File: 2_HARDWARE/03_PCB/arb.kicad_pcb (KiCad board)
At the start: 6 copper layers, 104.3 x 53.5 mm, 269 parts, among them J1 TYPE-C-31-M-12, J2 SMA, J3 SMA, J4 BNC, J5 PH-00244, SW1 TS-1187A-B-A-B, U1 TLV70333DBV, U10 LMK1C1103PWR, U11 STM32F446ZETx, U12 ICE40UP5K-SG48ITR, U13 93LC56BT-I_OT, U14 FT2232HL, U15 W25Q128JVSIQ, U16 W25Q128JVSIQ, U17 AD9850, U18 AD9744, U19 LM6171, U2 TLV76133DCY, U20 LM6171, U21 TMUX6104, U22 TPL0401B-10, U23 THS3491, U24 ADG1219BRJZ, U25 LM6171, U26 TMUX6104, U3 TLV70333DBV, U4 LM3880MF-1AA, U5 TLV70312DBV, U6 TLV70325DBV, U7 TPS65131RGE, U8 TPD2E001DRL, U9 ADG1219BRJZ, X1 ASE-10.000MHz, X2 ASE-100.000MHz, Y1 32.768k, Y2 12 MHz

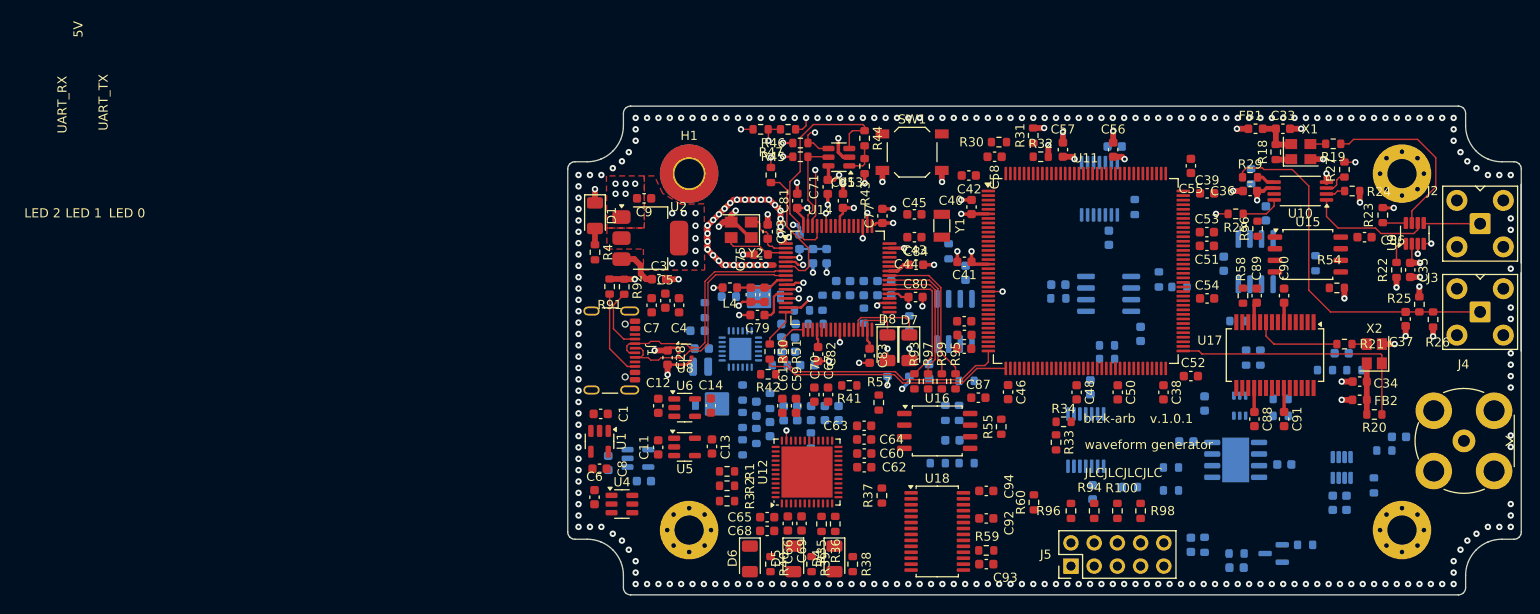
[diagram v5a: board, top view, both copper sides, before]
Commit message: MINOR: Added Power and GND Vias on the Top Layer.
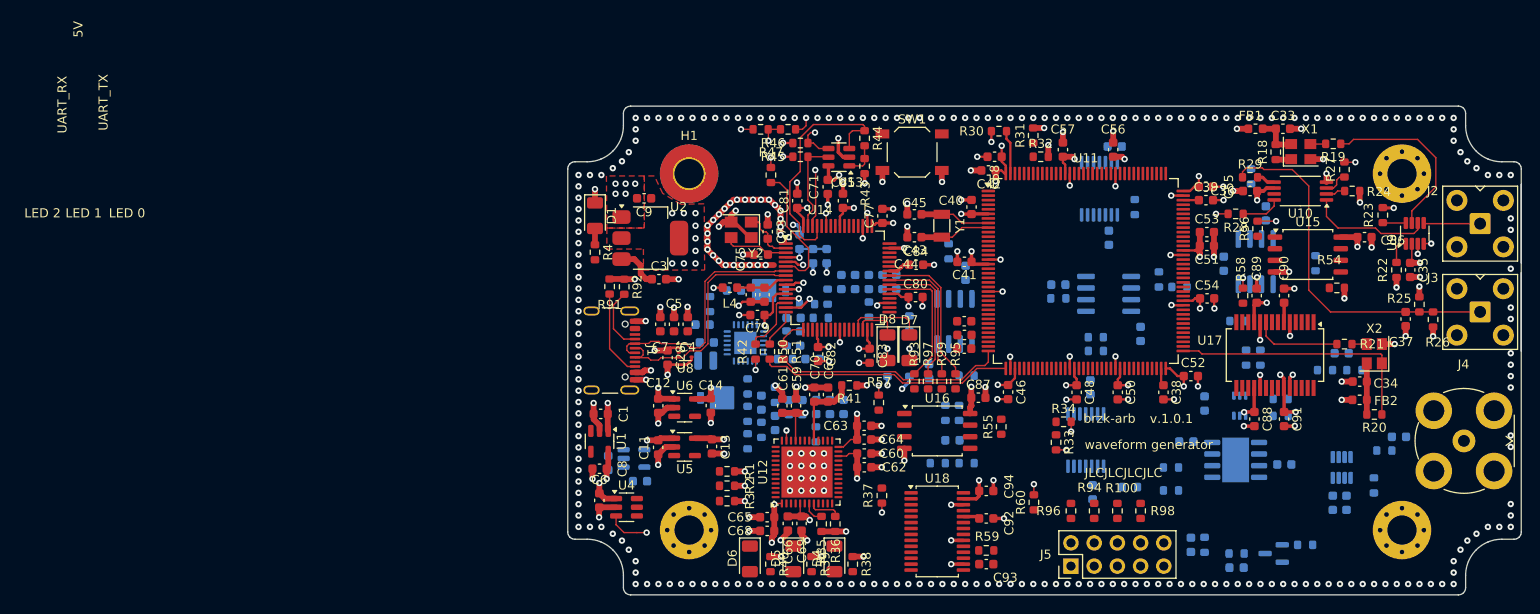
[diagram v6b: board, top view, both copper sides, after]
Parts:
- moved R42 2.83 mm to (116.4, 86.9), turned to 90 degrees
- moved C55 2.81 mm to (165.7, 68.8), turned to 0 degrees
- moved C5 2.74 mm to (107.5, 83.9)
- moved C4 2.28 mm to (109.0, 83.9)
- moved C7 2.28 mm to (106.0, 83.9)
- moved C42 2.22 mm to (141.8, 67.0)
- moved R85 1.51 mm to (153.6, 86.8)
- moved R88 1.51 mm to (153.6, 85.3)
- moved R30 1.20 mm to (143.0, 62.8)
- moved C16 0.87 mm to (110.6, 83.9)
- moved C25 0.87 mm to (127.3, 79.3)
- moved L1 0.87 mm to (110.9, 87.8)
- moved R17 0.87 mm to (128.8, 82.3)
- moved R5 0.87 mm to (111.4, 81.7)
- moved C19 0.87 mm to (117.0, 92.5)
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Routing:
- net GND: track 101.4 -> 193.0 mm, vias 303 -> 384
- net 3P3V_D: track 50.9 -> 115.4 mm, vias 32 -> 60
- net 3P3V_D_FPGA: track 0.00 -> 22.4 mm, vias 0 -> 7
- net 5P0V: track 8.85 -> 23.1 mm, vias 2 -> 7
- net Net-(U12D-VCCPLL): track 0.00 -> 8.57 mm
- net 1P2V_D: track 0.00 -> 8.39 mm, vias 0 -> 3
- net 2P5V_D: track 0.00 -> 8.13 mm, vias 0 -> 2
- net Net-(U11-PC15): track 0.00 -> 7.75 mm
- net Net-(U11-PC14): track 0.00 -> 7.71 mm
- net Net-(U14-~{RESET}): track 0.00 -> 6.80 mm
- net Net-(U11-PDR_ON): track 0.00 -> 4.81 mm
- net 3P3V_A: track 4.87 -> 8.92 mm, vias 0 -> 2
- net GPIO_FPGARST_MCU_FPGA_3P3_L: track 0.00 -> 3.54 mm
- net GPIO_CFG_DONE_FPGA_MCU_3P3: track 0.00 -> 2.43 mm
- net Net-(U11-VCAP_1): track 0.00 -> 1.94 mm
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
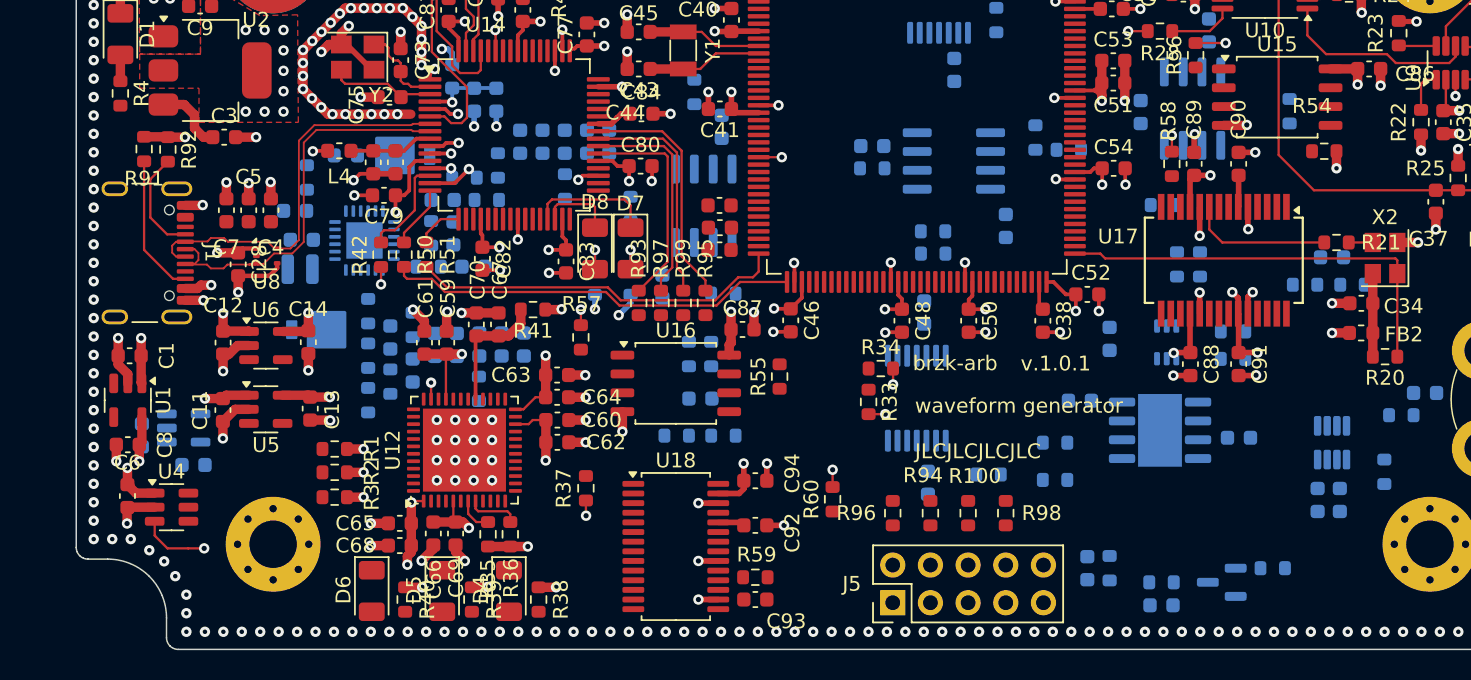
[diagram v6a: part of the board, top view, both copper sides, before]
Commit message: MINOR: Routed Layer 3 Power Planes.
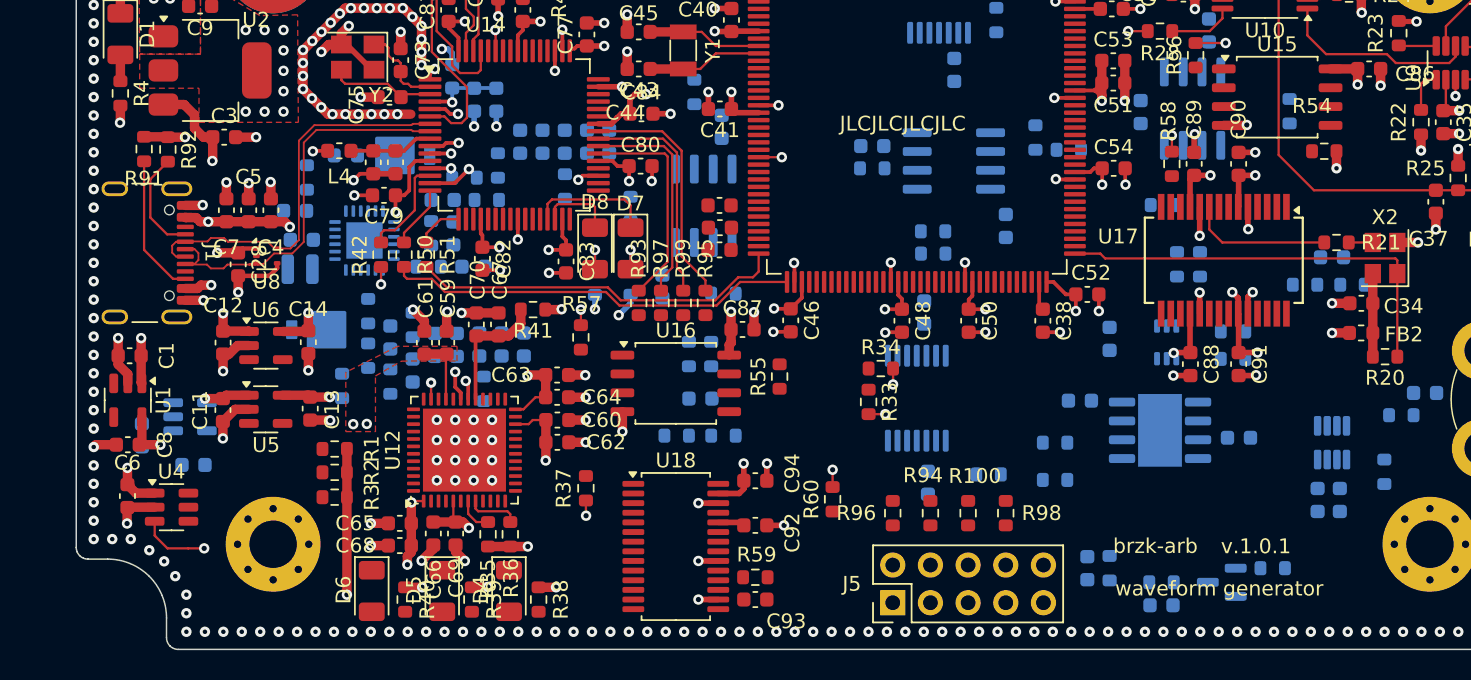
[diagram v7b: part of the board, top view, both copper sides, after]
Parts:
- moved R7 2.00 mm to (113.8, 95.7)
- moved U3 0.87 mm to (103.5, 97.8)
- moved R16 0.33 mm to (123.3, 95.9)
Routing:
- net 2P5V_D: track 8.13 -> 29.5 mm
- net 5P0V: track 23.1 -> 33.2 mm, vias 7 -> 11
- net 3P3V_D: track 115.4 -> 125.2 mm
- net GPIO_DACB4_FPGA_DAC_3P3: track 0.00 -> 1.99 mm, vias 0 -> 1
- net 1P2V_D: track 8.39 -> 9.68 mm, vias 3 -> 4
- net 3P3V_D_FPGA: track 22.4 -> 21.7 mm, vias 7 -> 8
- net CLK_10MHZ_DIST_MCU_3P3: track 54.8 -> 55.4 mm
- net GND: track 193.0 -> 193.5 mm, vias 384 -> 383
- added copper zone on In2.Cu, net 1P2V_D
- added copper zone on In2.Cu, net 3P3V_D
- added copper zone on F.Cu, net 3P3V_D_FPGA
- added copper zone on In2.Cu, net 3P3V_D_FPGA
- added copper zone on In2.Cu, net 5P0V
